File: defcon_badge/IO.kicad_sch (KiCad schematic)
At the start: 9 parts, among them J30 SAO 2x3, J31 microSD, J32 UART debug, SW20 TS-1187A, SW21 TS-1187A, SW22 TS-1187A, SW23 TS-1187A

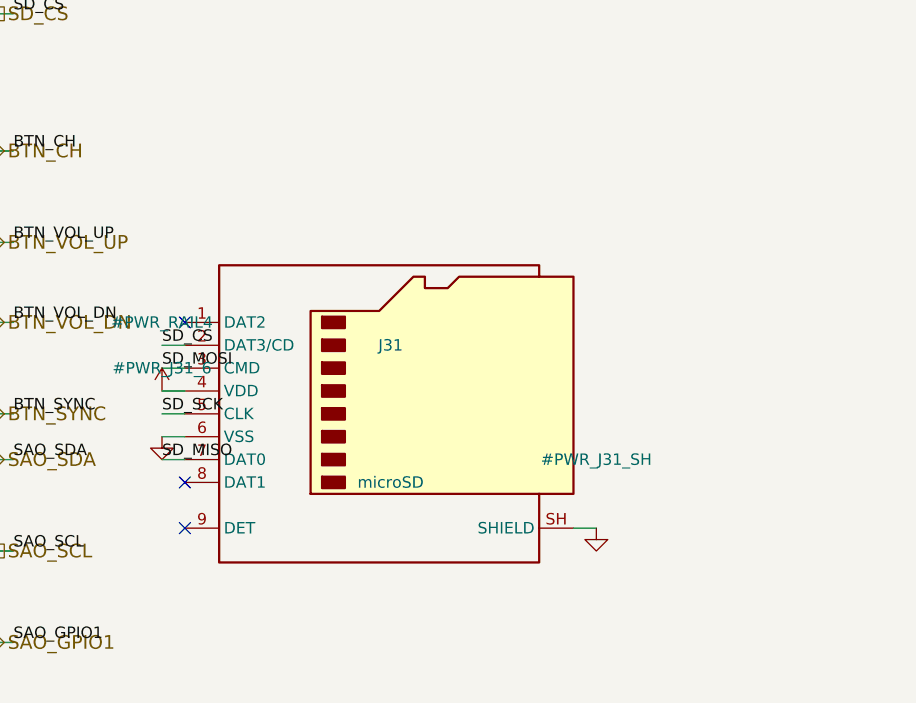
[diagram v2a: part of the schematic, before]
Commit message: Schematic: wire microSD card-detect (SD_CD) + add generator global-label support
Card-detect was unwired ("not wired this rev"). Wired it as a cross-sheet net:
- gen_io_sheet: J31.9 (DET) -> SD_CD with a 10k pull-up (R42) to +3V3. The DET
  switch shorts pin 9 to the grounded shield when a card is inserted, so SD_CD
  reads LOW = card present.
- MCU_Core: repurposed the GP22 spare (U3.34) for SD_CD.
- kicad_sheet_gen: add global-label support (global_label_at_pin / _render_global).
  Used a global label so SD_CD connects across the hierarchy without editing the
  top sheet's sheet-pins/wiring.

Verified: SD_CD = {J31.9, R42.1, U3.34}, R42.2->+3V3, ERC 0 errors.

SCHEMATIC COMPLETE: ERC 0 errors, all board-killers + subsystem-fatal bugs fixed,
4/5 sch_health gates pass (5th = waived GPIO spares). Remaining is the PCB phase.

Co-Authored-By: Claude Opus 4.8 (1M context) <noreply@anthropic.com>
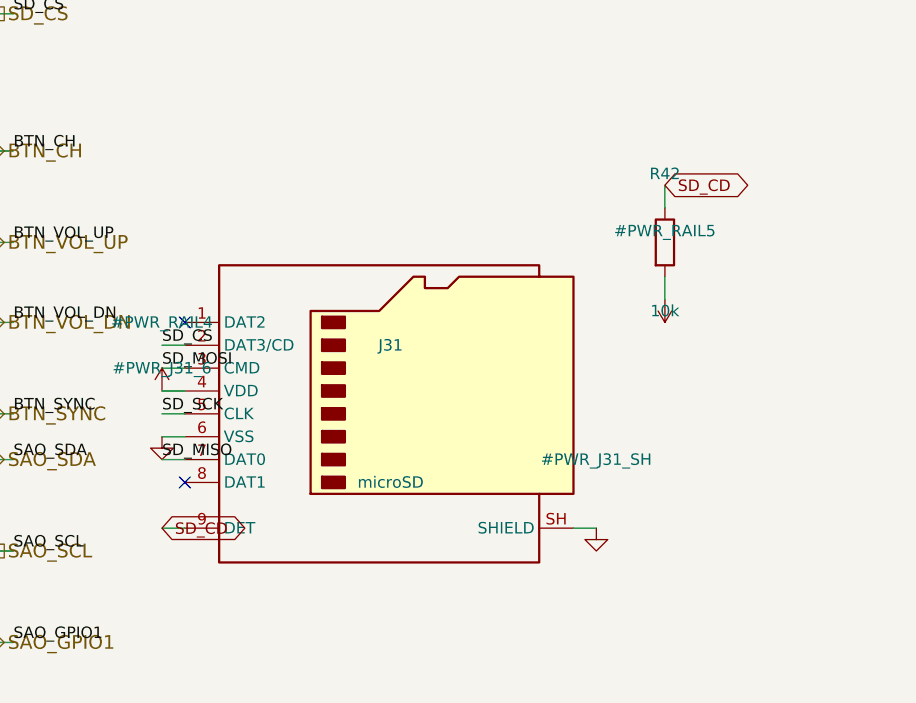
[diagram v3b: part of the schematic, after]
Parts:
- added R42: 10k, Resistor_SMD:R_0402_1005Metric, symbol Device:R
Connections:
- net +3V3: now also R42.2
- net SD_CD: now reaches J31.9 (DET)
- net SD_CD: now also R42.1
- no-connect marks 3 -> 2
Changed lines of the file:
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@@
+	)
+	(symbol
+		(lib_id "Device:R")
+		(at 110.49 110.49 0)
+		(unit 1)
+		(body_style 1)
+		(exclude_from_sim no)
+		(in_bom yes)
+		(on_board yes)
+		(in_pos_files yes)
+		(dnp no)
+		(fields_autoplaced yes)
+		(property "Reference" "R42" (at 110.49 102.87 0) (effects (font (size 1.27 1.27))))
+		(property "Value" "10k" (at 110.49 118.11 0) (effects (font (size 1.27 1.27))))
+		(property "Footprint" "Resistor_SMD:R_0402_1005Metric" (at 110.49 110.49 0) (show_name no) (hide yes) (effects (font (size 1.27 1.27))))
+		(property "Datasheet" "" (at 110.49 110.49 0) (show_name no) (hide yes) (effects (font (size 1.27 1.27))))
+		(property "Description" "microSD card-detect pull-up to +3V3" (at 110.49 110.49 0) (show_name no) (hide yes) (effects (font (size 1.27 1.27))))
+		(property "MPN" "RC0402FR-0710KL" (at 110.49 110.49 0) (show_name no) (hide yes) (effects (font (size 1.27 1.27))))
+		(property "LCSC" "C25744" (at 110.49 110.49 0) (show_name no) (hide yes) (effects (font (size 1.27 1.27))))
+		(pin "1")
+		(pin "2")
+		(instances
+			(project "defcon_badge"
+				(path "/8c0b3d8b-46d3-4173-ab1e-a61765f77d61/608539de-722a-4bca-b1da-2c313b60cd6f"
+					(reference "R42")
+					(unit 1)
+				)
+			)
+		)
+	)
+	(symbol
+		(lib_id "power:+3V3")
+		(at 110.49 116.84 180)
+		(unit 1)
+		(body_style 1)
+		(exclude_from_sim no)
+		(in_bom yes)
+		(on_board yes)
+		(in_pos_files yes)
+		(dnp no)
+		(fields_autoplaced yes)
+		(property "Reference" "#PWR_RAIL5" (at 110.49 109.22 0) (effects (font (size 1.27 1.27))))
+		(property "Value" "+3V3" (at 110.49 124.46 0) (effects (font (size 1.27 1.27)) (hide yes)))
+		(property "Footprint" "" (at 110.49 116.84 0) (show_name no) (hide yes) (effects (font (size 1.27 1.27))))
+		(property "Datasheet" "" (at 110.49 116.84 0) (show_name no) (hide yes) (effects (font (size 1.27 1.27))))
+		(property "Description" "" (at 110.49 116.84 0) (show_name no) (hide yes) (effects (font (size 1.27 1.27))))
+		(pin "1")
+		(instances
+			(project "defcon_badge"
+				(path "/8c0b3d8b-46d3-4173-ab1e-a61765f77d61/608539de-722a-4bca-b1da-2c313b60cd6f"
+					(reference "#PWR_RAIL5")
+					(unit 1)
+				)
+			)
+		)
 	)
 	(symbol
@@
 	(wire (pts (xy 57.15 132.08) (xy 54.61 132.08)) (stroke (width 0) (type default)))
 	(wire (pts (xy 57.15 134.62) (xy 54.61 134.62)) (stroke (width 0) (type default)))
+	(wire (pts (xy 57.15 142.24) (xy 54.61 142.24)) (stroke (width 0) (type default)))
 	(wire (pts (xy 100.33 142.24) (xy 102.87 142.24)) (stroke (width 0) (type default)))
+	(wire (pts (xy 110.49 106.68) (xy 110.49 104.14)) (stroke (width 0) (type default)))
+	(wire (pts (xy 110.49 114.30) (xy 110.49 116.84)) (stroke (width 0) (type default)))
 	(wire (pts (xy 194.31 127.00) (xy 191.77 127.00)) (stroke (width 0) (type default)))
 	(wire (pts (xy 194.31 129.54) (xy 191.77 129.54)) (stroke (width 0) (type default)))
@@
 	(no_connect (at 57.15 119.38))
 	(no_connect (at 57.15 137.16))
-	(no_connect (at 57.15 142.24))
 	(label "BTN_CH" (at 41.91 59.69 0) (effects (font (size 1.27 1.27)) (justify left bottom)))
 	(label "BTN_VOL_UP" (at 62.23 59.69 0) (effects (font (size 1.27 1.27)) (justify left bottom)))
@@
 	(hierarchical_label "UART_TX" (shape input) (at 35.56 180.34 0) (effects (font (size 1.524 1.524)) (justify left)))
 	(hierarchical_label "UART_RX" (shape output) (at 35.56 190.50 0) (effects (font (size 1.524 1.524)) (justify left)))
+	(global_label "SD_CD" (shape bidirectional) (at 54.61 142.24 0) (effects (font (size 1.27 1.27)) (justify left)))
+	(global_label "SD_CD" (shape bidirectional) (at 110.49 104.14 0) (effects (font (size 1.27 1.27)) (justify left)))
 	(sheet_instances
 		(path "/8c0b3d8b-46d3-4173-ab1e-a61765f77d61/608539de-722a-4bca-b1da-2c313b60cd6f"
